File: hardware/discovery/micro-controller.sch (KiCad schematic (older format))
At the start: 20 parts, among them U4 STM32F407VG, X1 CRYSTAL

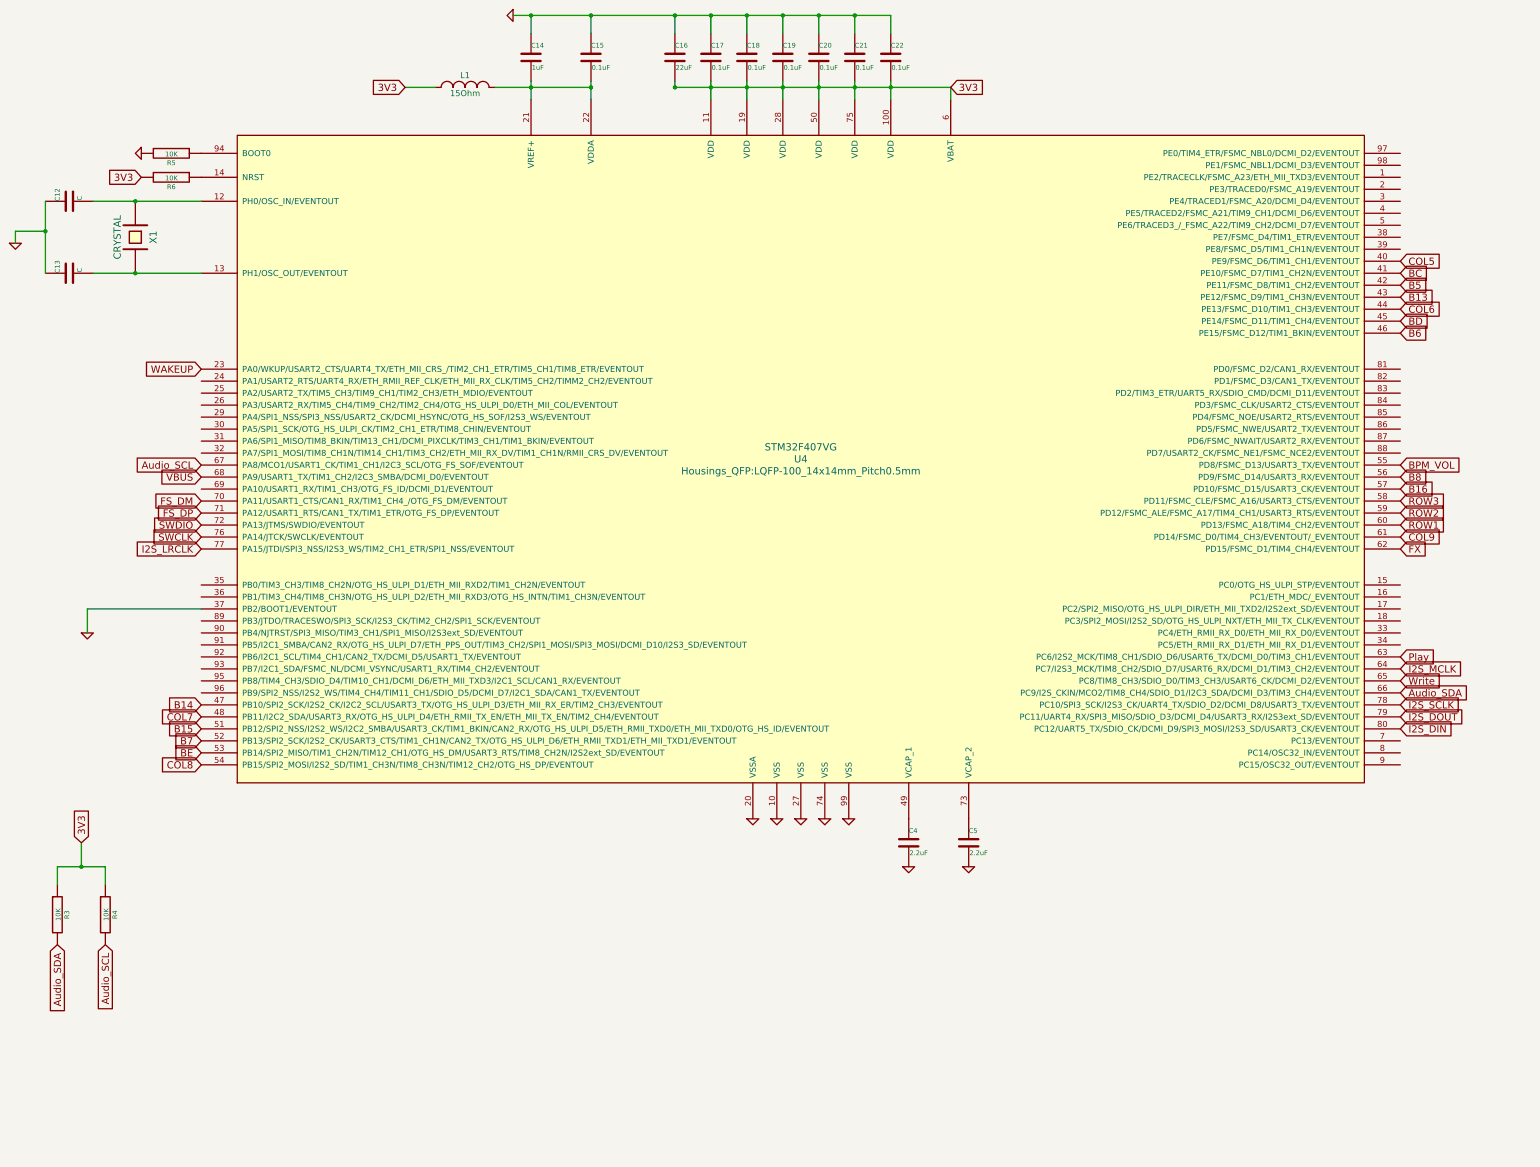
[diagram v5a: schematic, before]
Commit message: Discovery: Add micro SD card
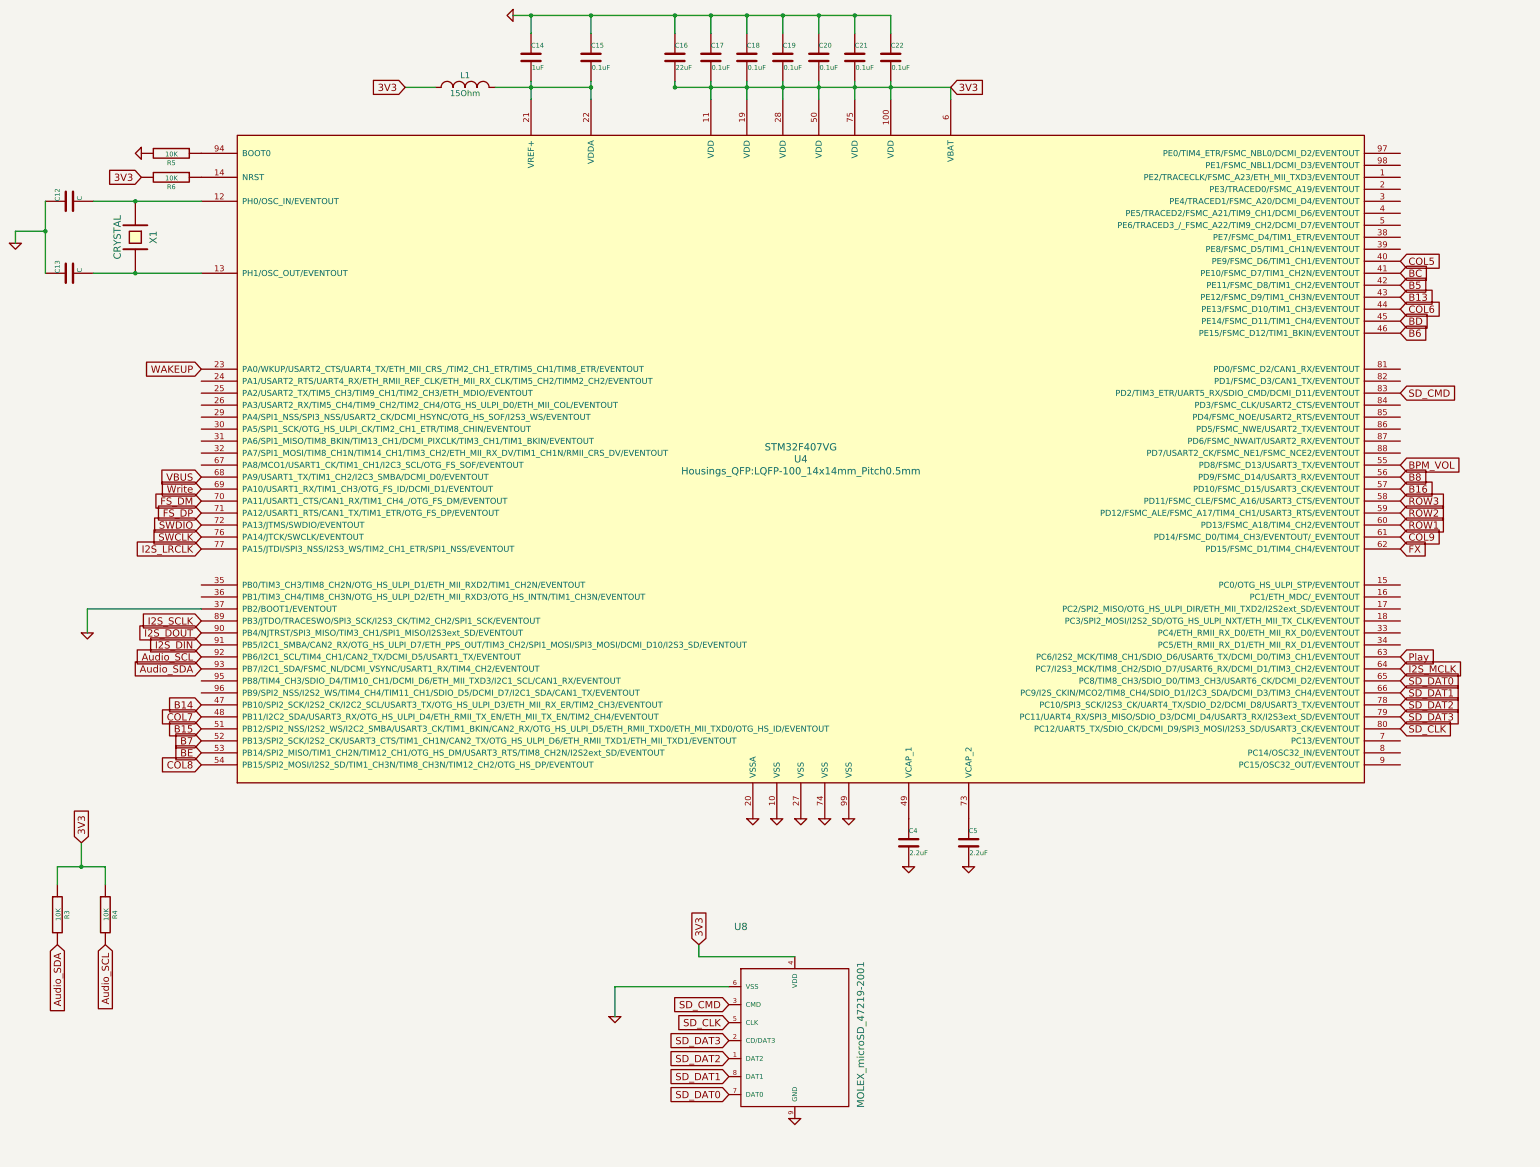
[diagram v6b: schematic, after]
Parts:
- added U8: MOLEX_microSD_47219-2001, stm32f4-disco:MOLEX_microSD_47219-2001, symbol MOLEX_microSD_47219-2001
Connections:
- net 3V3: now also U8.4 (VDD)
- net Audio_SCL: now also U4.92 (PB6/I2C1_SCL/TIM4_CH1/CAN2_TX/DCMI_D5/USART1_TX/EVENTOUT); no longer U4.67 (PA8/MCO1/USART1_CK/TIM1_CH1/I2C3_SCL/OTG_FS_SOF/EVENTOUT)
- net Audio_SDA: now also U4.93 (PB7/I2C1_SDA/FSMC_NL/DCMI_VSYNC/USART1_RX/TIM4_CH2/EVENTOUT); no longer U4.66 (PC9/I2S_CKIN/MCO2/TIM8_CH4/SDIO_D1/I2C3_SDA/DCMI_D3/TIM3_CH4/EVENTOUT)
- net GND: now also U8.6 (VSS), U8.9 (GND)
- net I2S_DIN: now also U4.91 (PB5/I2C1_SMBA/CAN2_RX/OTG_HS_ULPI_D7/ETH_PPS_OUT/TIM3_CH2/SPI1_MOSI/SPI3_MOSI/DCMI_D10/I2S3_SD/EVENTOUT); no longer U4.80 (PC12/UART5_TX/SDIO_CK/DCMI_D9/SPI3_MOSI/I2S3_SD/USART3_CK/EVENTOUT)
- net I2S_DOUT: now also U4.90 (PB4/NJTRST/SPI3_MISO/TIM3_CH1/SPI1_MISO/I2S3ext_SD/EVENTOUT); no longer U4.79 (PC11/UART4_RX/SPI3_MISO/SDIO_D3/DCMI_D4/USART3_RX/I2S3ext_SD/EVENTOUT)
- net I2S_SCLK: now also U4.89 (PB3/JTDO/TRACESWO/SPI3_SCK/I2S3_CK/TIM2_CH2/SPI1_SCK/EVENTOUT); no longer U4.78 (PC10/SPI3_SCK/I2S3_CK/UART4_TX/SDIO_D2/DCMI_D8/USART3_TX/EVENTOUT)
- net Write: now also U4.69 (PA10/USART1_RX/TIM1_CH3/OTG_FS_ID/DCMI_D1/EVENTOUT); no longer U4.65 (PC8/TIM8_CH3/SDIO_D0/TIM3_CH3/USART6_CK/DCMI_D2/EVENTOUT)
- net SD_CMD: now reaches U4.83 (PD2/TIM3_ETR/UART5_RX/SDIO_CMD/DCMI_D11/EVENTOUT)
- net SD_CMD: now also U8.3 (CMD)
- new net SD_CLK: U4.80 (PC12/UART5_TX/SDIO_CK/DCMI_D9/SPI3_MOSI/I2S3_SD/USART3_CK/EVENTOUT), U8.5 (CLK)
- new net SD_DAT0: U4.65 (PC8/TIM8_CH3/SDIO_D0/TIM3_CH3/USART6_CK/DCMI_D2/EVENTOUT), U8.7 (DAT0)
- new net SD_DAT1: U4.66 (PC9/I2S_CKIN/MCO2/TIM8_CH4/SDIO_D1/I2C3_SDA/DCMI_D3/TIM3_CH4/EVENTOUT), U8.8 (DAT1)
- new net SD_DAT2: U4.78 (PC10/SPI3_SCK/I2S3_CK/UART4_TX/SDIO_D2/DCMI_D8/USART3_TX/EVENTOUT), U8.1 (DAT2)
- new net SD_DAT3: U4.79 (PC11/UART4_RX/SPI3_MISO/SDIO_D3/DCMI_D4/USART3_RX/I2S3ext_SD/EVENTOUT), U8.2 (CD/DAT3)
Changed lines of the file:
@@
 Text GLabel 2850 5500 0    60   Input ~ 0
 SWCLK
-Text GLabel 2850 4900 0    60   Input ~ 0
+Text GLabel 2850 6500 0    60   Input ~ 0
 Audio_SCL
-Text GLabel 12850 6800 2    60   Input ~ 0
+Text GLabel 2850 6600 0    60   Input ~ 0
 Audio_SDA
-Text GLabel 12850 6900 2    60   Input ~ 0
+Text GLabel 2850 6200 0    60   Input ~ 0
 I2S_SCLK
-Text GLabel 12850 7000 2    60   Input ~ 0
+Text GLabel 2850 6300 0    60   Input ~ 0
 I2S_DOUT
-Text GLabel 12850 7100 2    60   Input ~ 0
+Text GLabel 2850 6400 0    60   Input ~ 0
 I2S_DIN
 Text GLabel 2850 5200 0    60   Input ~ 0
@@
 I2S_MCLK
 Text GLabel 12850 6700 2    60   Input ~ 0
-Write
+SD_DAT0
 Text GLabel 12850 6500 2    60   Input ~ 0
 Play
@@
 Text GLabel 12850 3200 2    60   Input ~ 0
 COL5
+$Comp
+L MOLEX_microSD_47219-2001 U8
+U 1 1 58639490
+P 7350 8750
+F 0 "U8" H 7350 8750 60  0000 C CNN
+F 1 "MOLEX_microSD_47219-2001" V 8350 7850 60  0000 C CNN
+F 2 "stm32f4-disco:MOLEX_microSD_47219-2001" H 7350 8750 60  0001 C CNN
+F 3 "" H 7350 8750 60  0001 C CNN
+	1    7350 8750
+	1    0    0    -1
+$EndComp
+$Comp
+L GND #PWR022
+U 1 1 586394FE
+P 7800 10350
+F 0 "#PWR022" H 7800 10350 30  0001 C CNN
+F 1 "GND" H 7800 10280 30  0001 C CNN
+F 2 "" H 7800 10350 60  0001 C CNN
+F 3 "" H 7800 10350 60  0001 C CNN
+	1    7800 10350
+	1    0    0    -1
+$EndComp
+Text GLabel 7250 9850 0    60   Input ~ 0
+SD_DAT2
+Text GLabel 7250 9700 0    60   Input ~ 0
+SD_DAT3
+Text GLabel 7250 9400 0    60   Input ~ 0
+SD_CMD
+Text GLabel 7250 9550 0    60   Input ~ 0
+SD_CLK
+Text GLabel 7250 10150 0    60   Input ~ 0
+SD_DAT0
+Text GLabel 7250 10000 0    60   Input ~ 0
+SD_DAT1
+Wire Wire Line
+	7000 9000 7800 9000
+Wire Wire Line
+	7000 9000 7000 8900
+Text GLabel 7000 8900 1    60   Input ~ 0
+3V3
+Text GLabel 12850 7000 2    60   Input ~ 0
+SD_DAT3
+Text GLabel 12850 6800 2    60   Input ~ 0
+SD_DAT1
+Text GLabel 12850 6900 2    60   Input ~ 0
+SD_DAT2
+Text GLabel 2850 5100 0    60   Input ~ 0
+Write
+Text GLabel 12850 7100 2    60   Input ~ 0
+SD_CLK
+Text GLabel 12850 4300 2    60   Input ~ 0
+SD_CMD
+Wire Wire Line
+	7250 9250 6300 9250
+Wire Wire Line
+	6300 9250 6300 9500
+$Comp
+L GND #PWR?
+U 1 1 58631320
+P 6300 9500
+F 0 "#PWR?" H 6300 9500 30  0001 C CNN
+F 1 "GND" H 6300 9430 30  0001 C CNN
+F 2 "" H 6300 9500 60  0001 C CNN
+F 3 "" H 6300 9500 60  0001 C CNN
+	1    6300 9500
+	1    0    0    -1
+$EndComp
 $EndSCHEMATC

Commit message: Discovery: End of LEDs and buttons routing
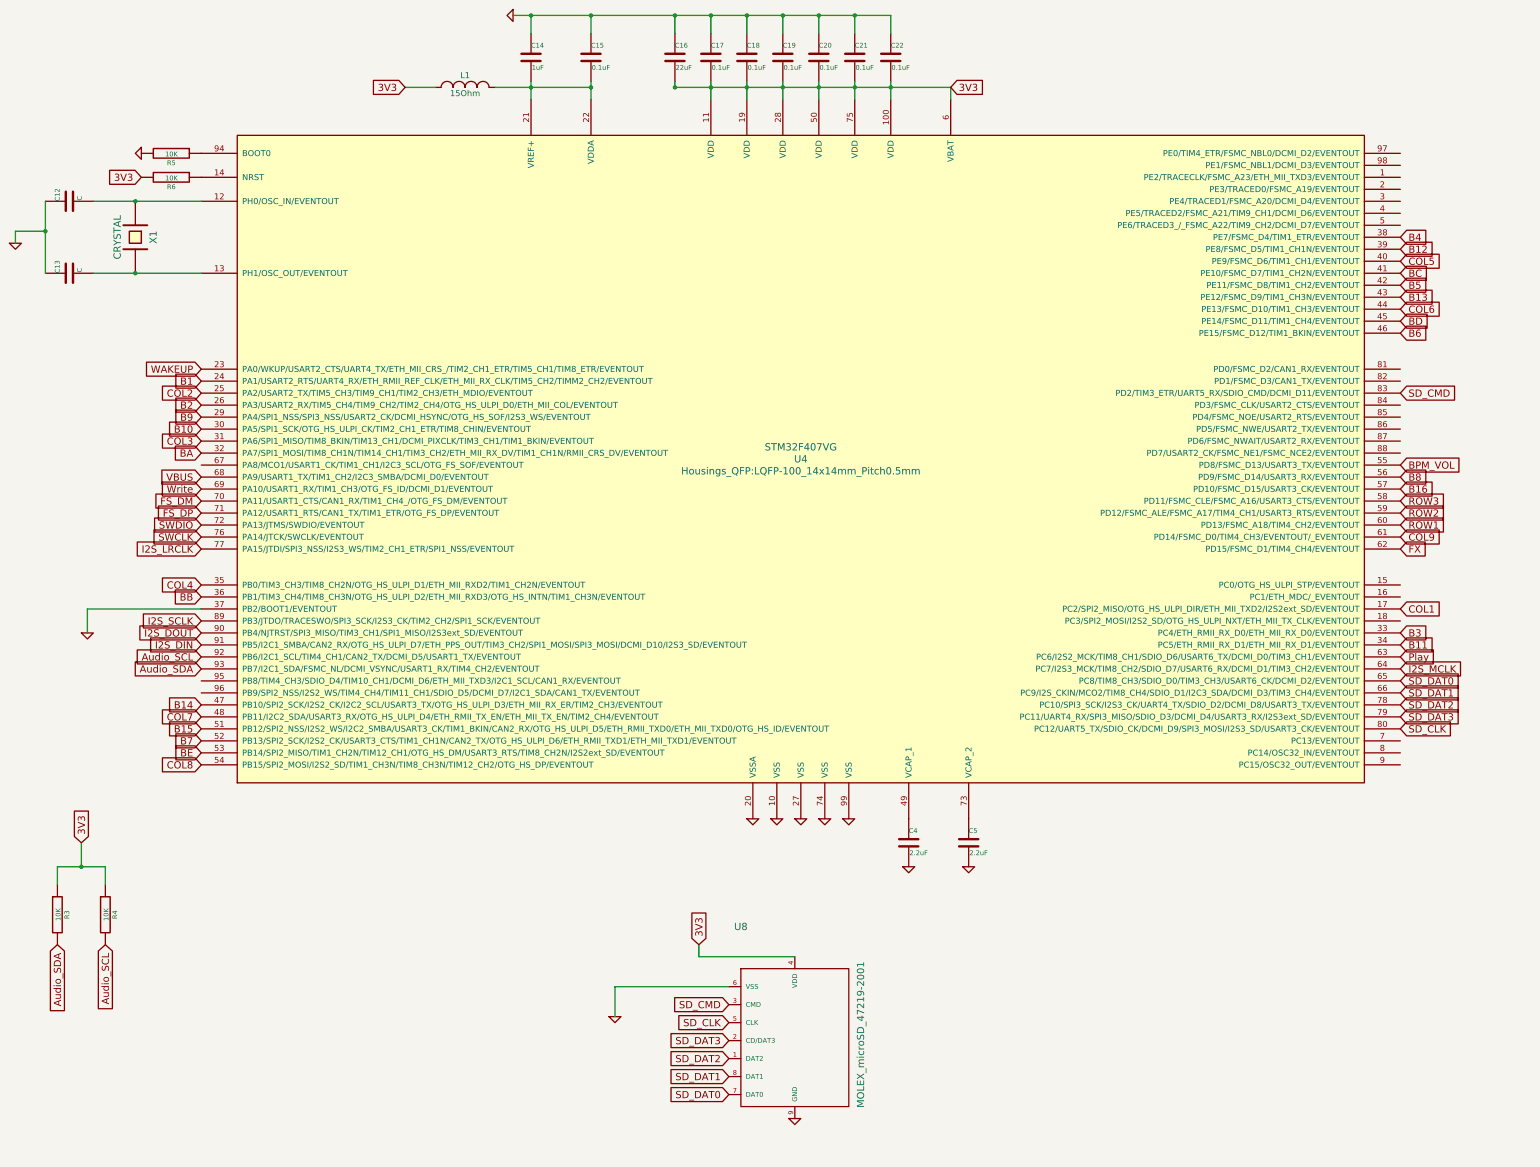
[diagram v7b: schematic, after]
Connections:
- net COL1: now reaches U4.17 (PC2/SPI2_MISO/OTG_HS_ULPI_DIR/ETH_MII_TXD2/I2S2ext_SD/EVENTOUT)
- net B1: now reaches U4.24 (PA1/USART2_RTS/UART4_RX/ETH_RMII_REF_CLK/ETH_MII_RX_CLK/TIM5_CH2/TIMM2_CH2/EVENTOUT)
- net COL2: now reaches U4.25 (PA2/USART2_TX/TIM5_CH3/TIM9_CH1/TIM2_CH3/ETH_MDIO/EVENTOUT)
- net B2: now reaches U4.26 (PA3/USART2_RX/TIM5_CH4/TIM9_CH2/TIM2_CH4/OTG_HS_ULPI_D0/ETH_MII_COL/EVENTOUT)
- net B9: now reaches U4.29 (PA4/SPI1_NSS/SPI3_NSS/USART2_CK/DCMI_HSYNC/OTG_HS_SOF/I2S3_WS/EVENTOUT)
- net B10: now reaches U4.30 (PA5/SPI1_SCK/OTG_HS_ULPI_CK/TIM2_CH1_ETR/TIM8_CHIN/EVENTOUT)
- net COL3: now reaches U4.31 (PA6/SPI1_MISO/TIM8_BKIN/TIM13_CH1/DCMI_PIXCLK/TIM3_CH1/TIM1_BKIN/EVENTOUT)
- net BA: now reaches U4.32 (PA7/SPI1_MOSI/TIM8_CH1N/TIM14_CH1/TIM3_CH2/ETH_MII_RX_DV/TIM1_CH1N/RMII_CRS_DV/EVENTOUT)
- net B3: now reaches U4.33 (PC4/ETH_RMII_RX_D0/ETH_MII_RX_D0/EVENTOUT)
- net B11: now reaches U4.34 (PC5/ETH_RMII_RX_D1/ETH_MII_RX_D1/EVENTOUT)
- net COL4: now reaches U4.35 (PB0/TIM3_CH3/TIM8_CH2N/OTG_HS_ULPI_D1/ETH_MII_RXD2/TIM1_CH2N/EVENTOUT)
- net BB: now reaches U4.36 (PB1/TIM3_CH4/TIM8_CH3N/OTG_HS_ULPI_D2/ETH_MII_RXD3/OTG_HS_INTN/TIM1_CH3N/EVENTOUT)
- net B4: now reaches U4.38 (PE7/FSMC_D4/TIM1_ETR/EVENTOUT)
- net B12: now reaches U4.39 (PE8/FSMC_D5/TIM1_CH1N/EVENTOUT)
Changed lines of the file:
@@
 	6300 9250 6300 9500
 $Comp
-L GND #PWR?
+L GND #PWR023
 U 1 1 58631320
 P 6300 9500
-F 0 "#PWR?" H 6300 9500 30  0001 C CNN
+F 0 "#PWR023" H 6300 9500 30  0001 C CNN
 F 1 "GND" H 6300 9430 30  0001 C CNN
 F 2 "" H 6300 9500 60  0001 C CNN
@@
 	1    0    0    -1
 $EndComp
+Text GLabel 12850 3100 2    60   Input ~ 0
+B12
+Text GLabel 12850 3000 2    60   Input ~ 0
+B4
+Text GLabel 2850 6000 0    60   Input ~ 0
+BB
+Text GLabel 2850 5900 0    60   Input ~ 0
+COL4
+Text GLabel 12850 6400 2    60   Input ~ 0
+B11
+Text GLabel 12850 6300 2    60   Input ~ 0
+B3
+Text GLabel 2850 4800 0    60   Input ~ 0
+BA
+Text GLabel 2850 4700 0    60   Input ~ 0
+COL3
+Text GLabel 2850 4600 0    60   Input ~ 0
+B10
+Text GLabel 2850 4500 0    60   Input ~ 0
+B9
+Text GLabel 2850 4400 0    60   Input ~ 0
+B2
+Text GLabel 2850 4300 0    60   Input ~ 0
+COL2
+Text GLabel 2850 4200 0    60   Input ~ 0
+B1
+Text GLabel 12850 6100 2    60   Input ~ 0
+COL1
 $EndSCHEMATC

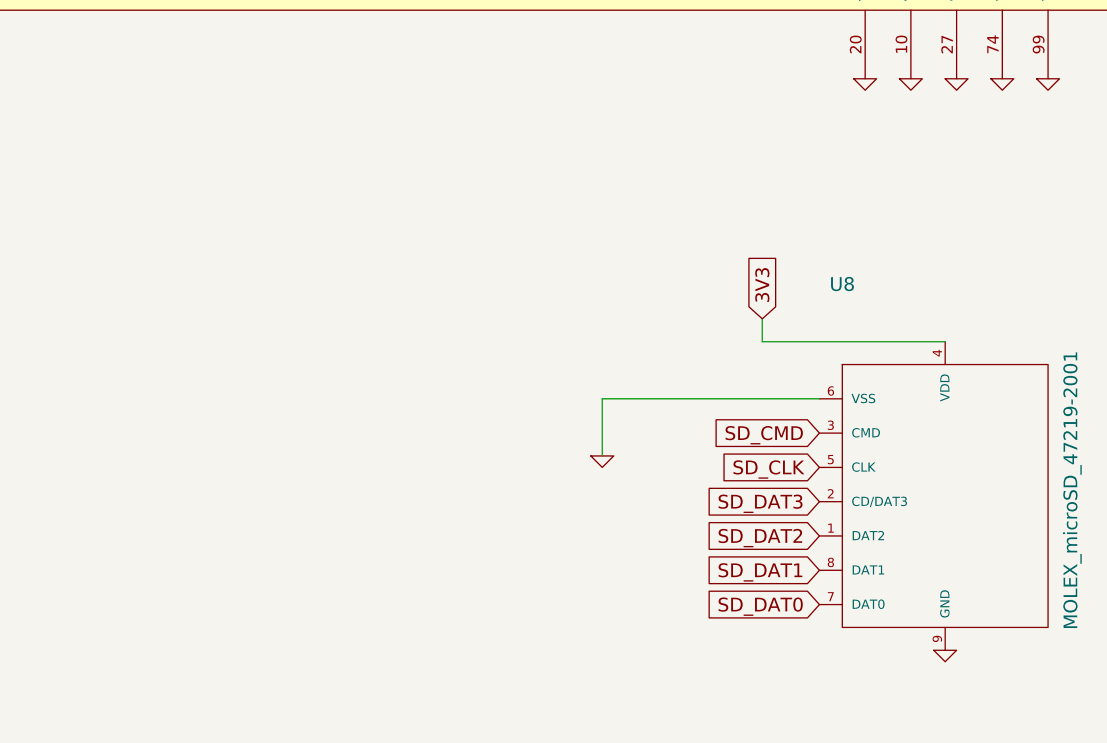
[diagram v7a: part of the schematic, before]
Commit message: Discovery: Move SD card socket
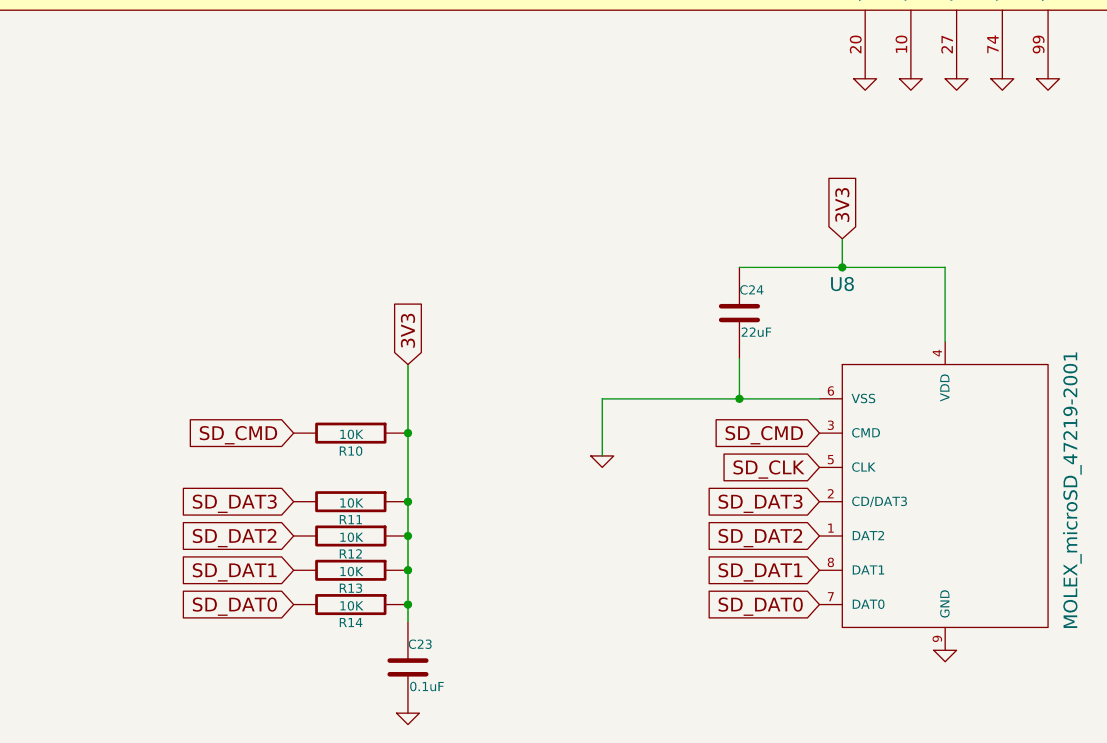
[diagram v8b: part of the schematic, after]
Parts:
- added C23: 0.1uF, Capacitors_SMD:C_0805, symbol C
- added C24: 22uF, Capacitors_SMD:C_0805, symbol C
- added R10, R11, R12, R13, R14: 10K, Resistors_SMD:R_0805, symbol R
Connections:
- net 3V3: now also C23.1, C24.1, R10.1, R11.1, R12.1, R13.1, R14.1
- net GND: now also C23.2, C24.2
- net SD_CMD: now also R10.2
- net SD_DAT0: now also R14.2
- net SD_DAT1: now also R13.2
- net SD_DAT2: now also R12.2
- net SD_DAT3: now also R11.2
